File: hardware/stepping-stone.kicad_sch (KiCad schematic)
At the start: 0 parts

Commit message: Add MCU and USB symbols
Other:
- added sheet Microcontroller (microcontroller.kicad_sch)
- added sheet USB-C Interface (usb-interface.kicad_sch)
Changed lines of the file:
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@@
 	(generator_version "10.0")
 	(paper "A")
+	(sheet
+		(at 76.2 88.9)
+		(size 25.4 25.4)
+		(exclude_from_sim no)
+		(in_bom yes)
+		(on_board yes)
+		(dnp no)
+		(fields_autoplaced yes)
+		(stroke
+			(width 0.3048)
+			(type solid)
+		)
+		(fill
+			(color 255 229 191 1)
+		)
+		(property "Sheetname" "USB-C Interface"
+			(at 76.2 88.1122 0)
+			(show_name no)
+			(do_not_autoplace no)
+			(effects
+				(font
+					(size 1.27 1.27)
+				)
+				(justify left bottom)
+			)
+		)
+		(property "Sheetfile" "usb-interface.kicad_sch"
+			(at 76.2 114.9608 0)
+			(show_name no)
+			(do_not_autoplace no)
+			(effects
+				(font
+					(size 1.27 1.27)
+				)
+				(justify left top)
+			)
+		)
+		(instances
+			(project "stepping-stone"
+				(path "/793a882e-3f7b-468b-a863-41a1f527e1bf"
+					(page "3")
+				)
+			)
+		)
+	)
+	(sheet
+		(at 127 88.9)
+		(size 25.4 25.4)
+		(exclude_from_sim no)
+		(in_bom yes)
+		(on_board yes)
+		(dnp no)
+		(fields_autoplaced yes)
+		(stroke
+			(width 0.3048)
+			(type solid)
+		)
+		(fill
+			(color 255 229 191 1)
+		)
+		(property "Sheetname" "Microcontroller"
+			(at 127 88.1122 0)
+			(show_name no)
+			(do_not_autoplace no)
+			(effects
+				(font
+					(size 1.27 1.27)
+				)
+				(justify left bottom)
+			)
+		)
+		(property "Sheetfile" "microcontroller.kicad_sch"
+			(at 127 114.9608 0)
+			(show_name no)
+			(do_not_autoplace no)
+			(effects
+				(font
+					(size 1.27 1.27)
+				)
+				(justify left top)
+			)
+		)
+		(instances
+			(project "stepping-stone"
+				(path "/793a882e-3f7b-468b-a863-41a1f527e1bf"
+					(page "2")
+				)
+			)
+		)
+	)
 	(sheet_instances
 		(path "/"

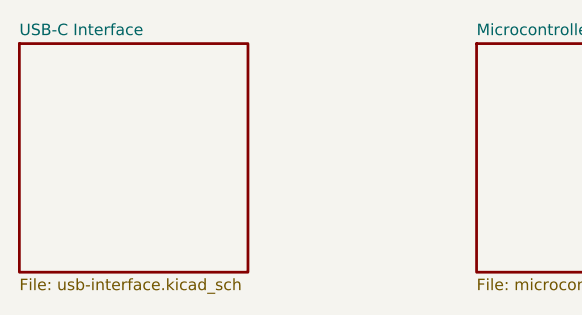
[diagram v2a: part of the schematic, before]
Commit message: Draft power inputs sheet
Added USB C PD input and external supply, with ideal diode ORing.
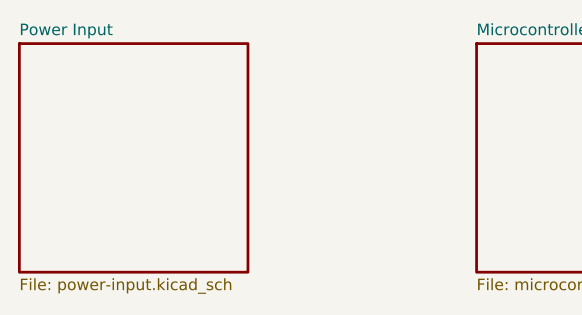
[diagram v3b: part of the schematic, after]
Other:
- sheet USB-C Interface renamed Power Input
- sheet Power Input: file usb-interface.kicad_sch -> power-input.kicad_sch
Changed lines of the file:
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@@
 			(color 255 229 191 1)
 		)
-		(property "Sheetname" "USB-C Interface"
+		(property "Sheetname" "Power Input"
 			(at 76.2 88.1122 0)
 			(show_name no)
@@
 			)
 		)
-		(property "Sheetfile" "usb-interface.kicad_sch"
+		(property "Sheetfile" "power-input.kicad_sch"
 			(at 76.2 114.9608 0)
 			(show_name no)

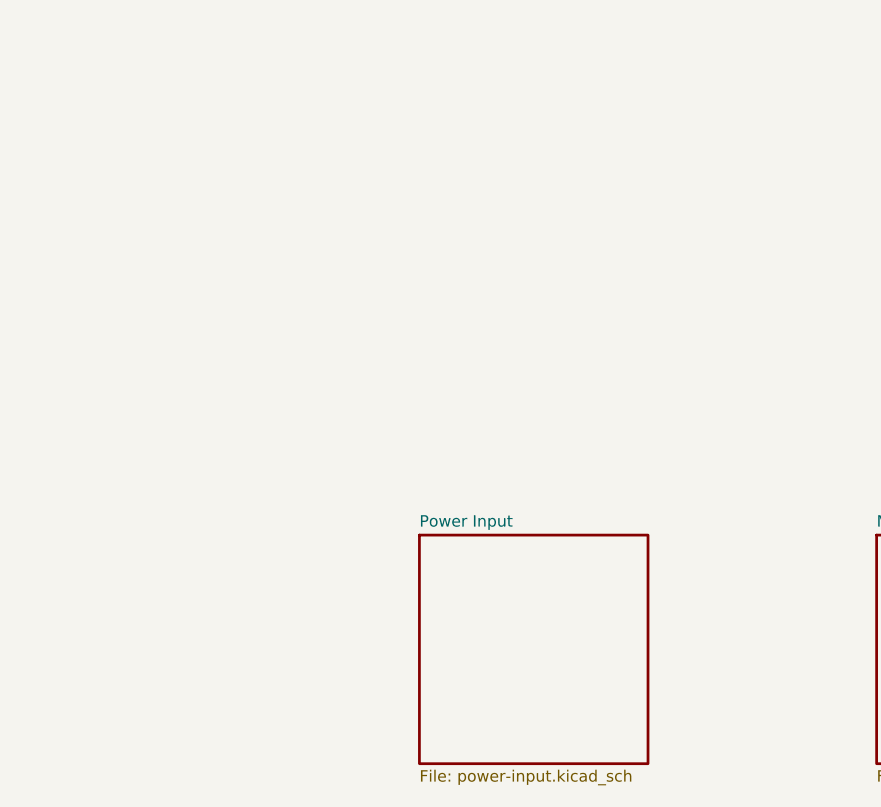
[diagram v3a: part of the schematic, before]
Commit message: Finalize source select
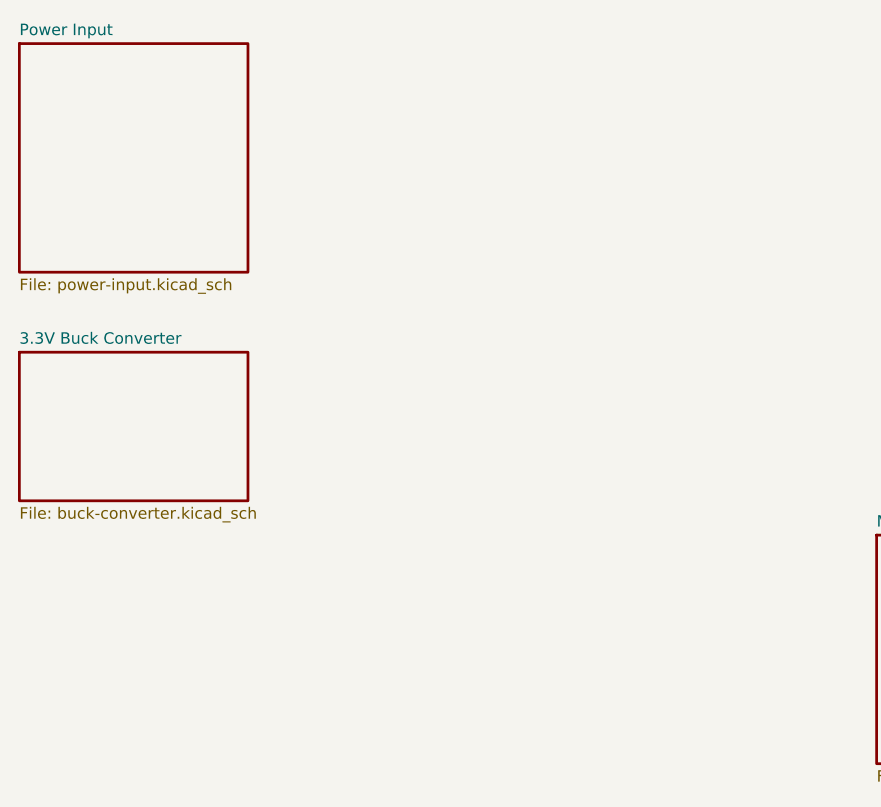
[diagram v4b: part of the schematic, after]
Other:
- added sheet 3.3V Buck Converter (buck-converter.kicad_sch)
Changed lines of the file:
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@@
 	(paper "A")
 	(sheet
-		(at 76.2 88.9)
+		(at 31.75 34.29)
 		(size 25.4 25.4)
 		(exclude_from_sim no)
@@
 		)
 		(property "Sheetname" "Power Input"
-			(at 76.2 88.1122 0)
+			(at 31.75 33.5022 0)
 			(show_name no)
 			(do_not_autoplace no)
@@
 		)
 		(property "Sheetfile" "power-input.kicad_sch"
-			(at 76.2 114.9608 0)
+			(at 31.75 60.3508 0)
 			(show_name no)
 			(do_not_autoplace no)
@@
 				)
 			)
+		)
+	)
+	(sheet
+		(at 31.75 68.58)
+		(size 25.4 16.51)
+		(exclude_from_sim no)
+		(in_bom yes)
+		(on_board yes)
+		(dnp no)
+		(fields_autoplaced yes)
+		(stroke
+			(width 0.3048)
+			(type solid)
+		)
+		(fill
+			(color 255 229 191 1)
+		)
+		(property "Sheetname" "3.3V Buck Converter"
+			(at 31.75 67.7922 0)
+			(show_name no)
+			(do_not_autoplace no)
+			(effects
+				(font
+					(size 1.27 1.27)
+				)
+				(justify left bottom)
+			)
+		)
+		(property "Sheetfile" "buck-converter.kicad_sch"
+			(at 31.75 85.7508 0)
+			(show_name no)
+			(do_not_autoplace no)
+			(effects
+				(font
+					(size 1.27 1.27)
+				)
+				(justify left top)
+			)
+		)
+		(instances
+			(project "stepping-stone"
+				(path "/793a882e-3f7b-468b-a863-41a1f527e1bf"
+					(page "4")
+				)
+			)

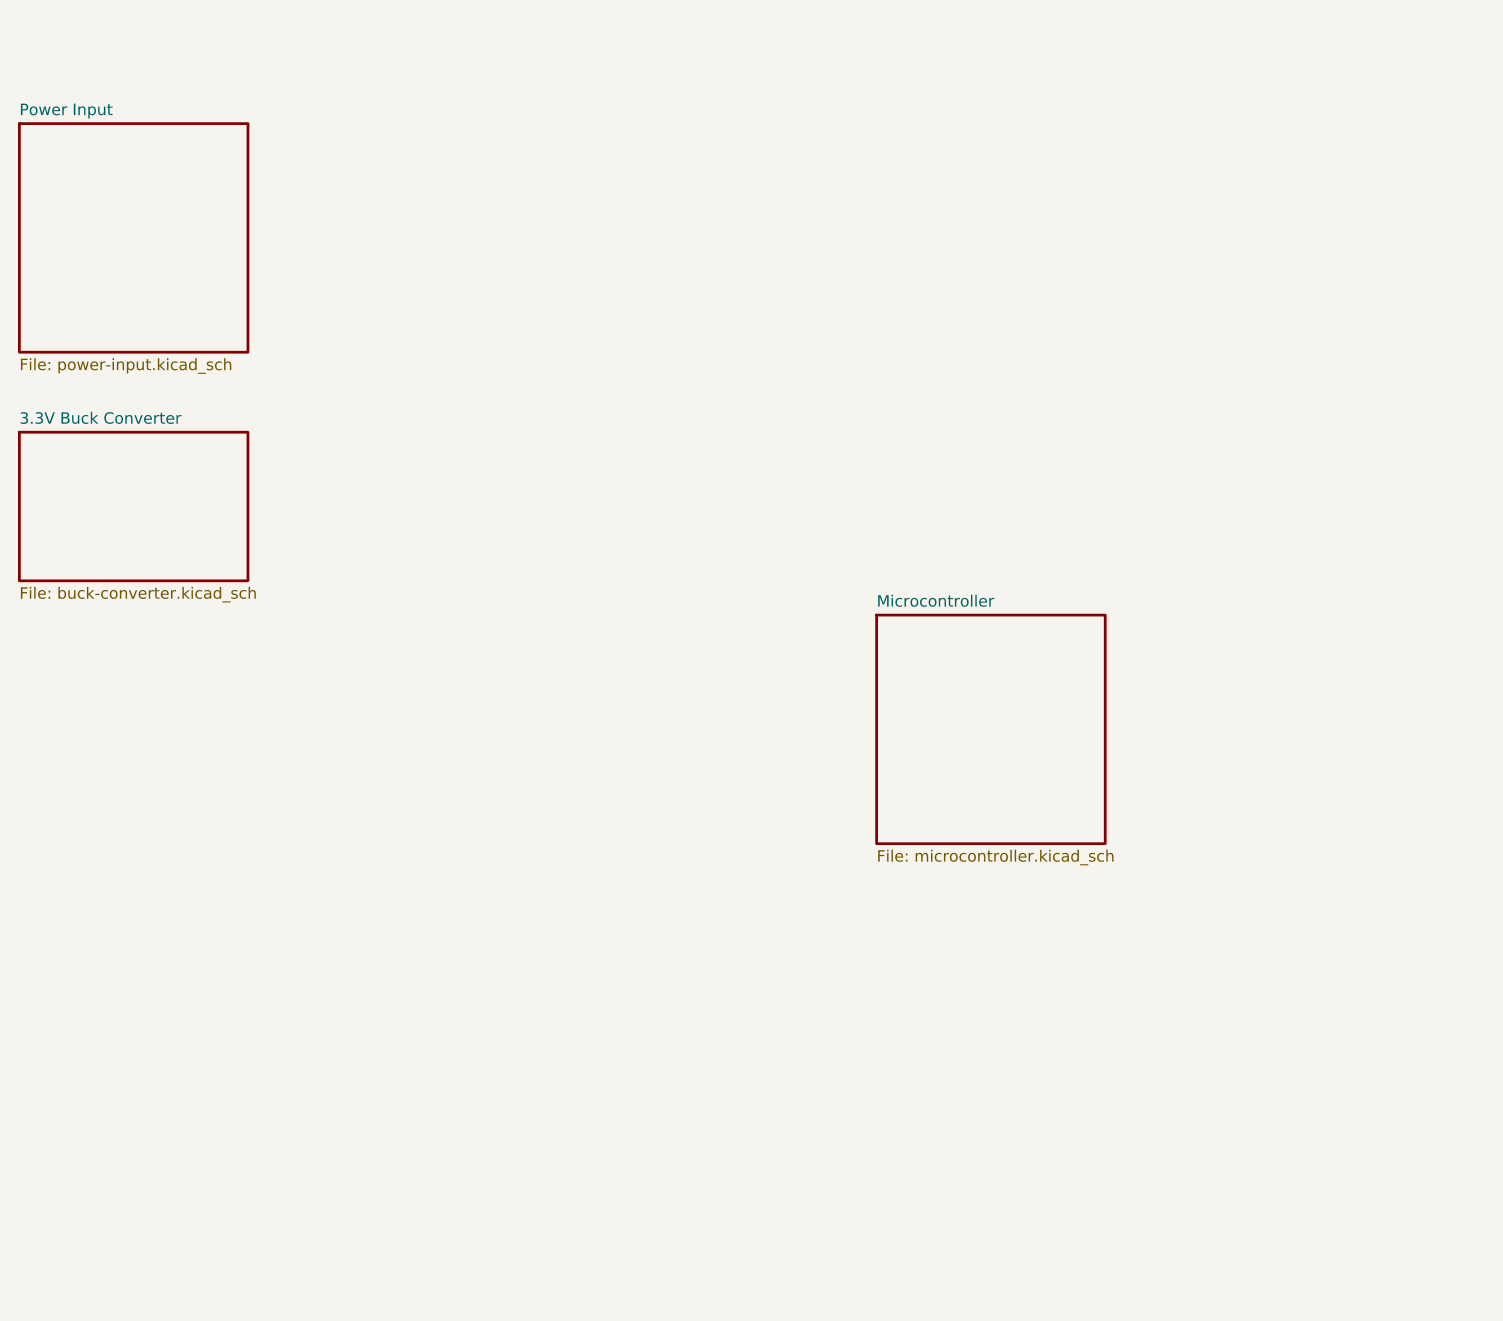
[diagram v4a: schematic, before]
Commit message: Add 3.3V buck converter
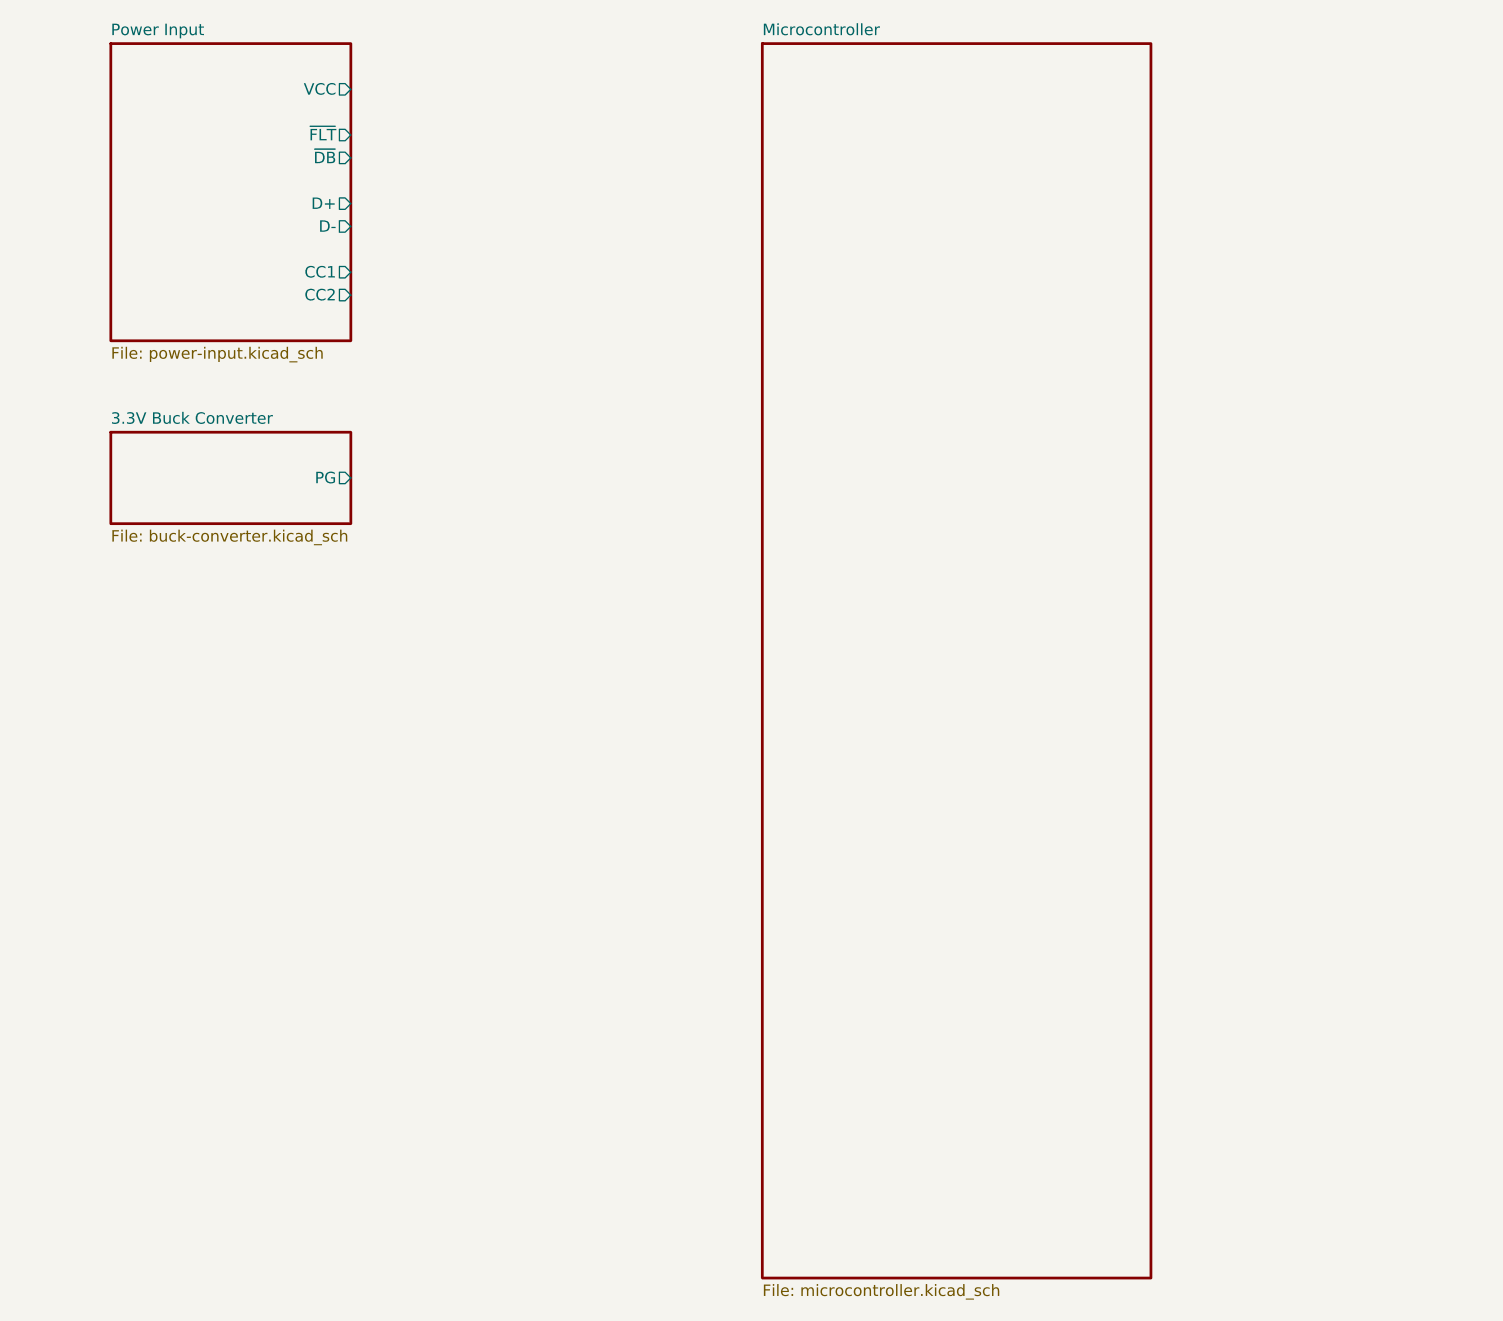
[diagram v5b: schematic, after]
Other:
- sheet 3.3V Buck Converter ports: added PG; removed none
- sheet Power Input ports: added CC1, CC2, D+, D-, VCC, ~{DB}, ~{FLT}; removed none
- company: (none) -> Jacob Wigent
- title: (none) -> Stepping-Stone - Stepper Motor Platform
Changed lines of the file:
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@@
 	(generator_version "10.0")
 	(paper "A")
+	(title_block
+		(title "Stepping-Stone - Stepper Motor Platform")
+		(rev "A")
+		(company "Jacob Wigent")
+	)
 	(sheet
-		(at 31.75 34.29)
-		(size 25.4 25.4)
+		(at 41.91 25.4)
+		(size 26.67 33.02)
 		(exclude_from_sim no)
 		(in_bom yes)
@@
 		)
 		(property "Sheetname" "Power Input"
-			(at 31.75 33.5022 0)
+			(at 41.91 24.6122 0)
 			(show_name no)
 			(do_not_autoplace no)
@@
 		)
 		(property "Sheetfile" "power-input.kicad_sch"
-			(at 31.75 60.3508 0)
+			(at 41.91 59.0808 0)
 			(show_name no)
 			(do_not_autoplace no)
@@
 				)
 				(justify left top)
+			)
+		)
+		(pin "CC1" output
+			(at 68.58 50.8 0)
+			(effects
+				(font
+					(size 1.27 1.27)
+				)
+				(justify right)
+			)
+		)
+		(pin "CC2" output
+			(at 68.58 53.34 0)
+			(effects
+				(font
+					(size 1.27 1.27)
+				)
+				(justify right)
+			)
+		)
+		(pin "D+" output
+			(at 68.58 43.18 0)
+			(effects
+				(font
+					(size 1.27 1.27)
+				)
+				(justify right)
+			)
+		)
+		(pin "D-" output
+			(at 68.58 45.72 0)
+			(effects
+				(font
+					(size 1.27 1.27)
+				)
+				(justify right)
+			)
+		)
+		(pin "VCC" output
+			(at 68.58 30.48 0)
+			(effects
+				(font
+					(size 1.27 1.27)
+				)
+				(justify right)
+			)
+		)
+		(pin "~{DB}" output
+			(at 68.58 38.1 0)
+			(effects
+				(font
+					(size 1.27 1.27)
+				)
+				(justify right)
+			)
+		)
+		(pin "~{FLT}" output
+			(at 68.58 35.56 0)
+			(effects
+				(font
+					(size 1.27 1.27)
+				)
+				(justify right)
 			)
 		)
@@
 	)
 	(sheet
-		(at 127 88.9)
-		(size 25.4 25.4)
+		(at 114.3 25.4)
+		(size 43.18 137.16)
 		(exclude_from_sim no)
 		(in_bom yes)
@@
 		)
 		(property "Sheetname" "Microcontroller"
-			(at 127 88.1122 0)
+			(at 114.3 24.6122 0)
 			(show_name no)
 			(do_not_autoplace no)
@@
 		)
 		(property "Sheetfile" "microcontroller.kicad_sch"
-			(at 127 114.9608 0)
+			(at 114.3 163.2208 0)
 			(show_name no)
 			(do_not_autoplace no)
@@
 	)
 	(sheet
-		(at 31.75 68.58)
-		(size 25.4 16.51)
+		(at 41.91 68.58)
+		(size 26.67 10.16)
 		(exclude_from_sim no)
 		(in_bom yes)
@@
 		)
 		(property "Sheetname" "3.3V Buck Converter"
-			(at 31.75 67.7922 0)
+			(at 41.91 67.7922 0)
 			(show_name no)
 			(do_not_autoplace no)
@@
 		)
 		(property "Sheetfile" "buck-converter.kicad_sch"
-			(at 31.75 85.7508 0)
+			(at 41.91 79.4008 0)
 			(show_name no)
 			(do_not_autoplace no)
@@
 			)
 		)
+		(pin "PG" output
+			(at 68.58 73.66 0)
+			(effects
+				(font
+					(size 1.27 1.27)
+				)
+				(justify right)
+			)
+		)

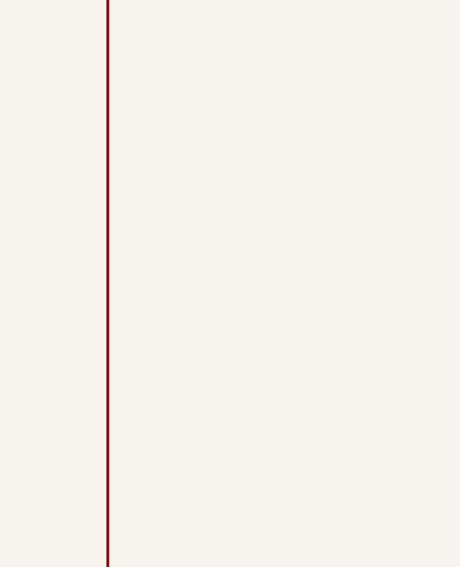
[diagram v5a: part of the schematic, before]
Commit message: Create MCU schematic
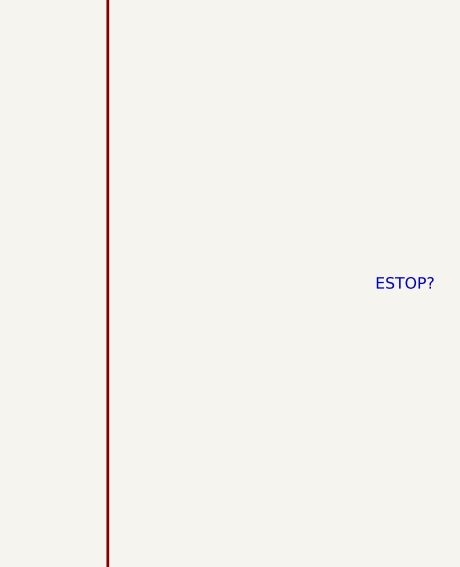
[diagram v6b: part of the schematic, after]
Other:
- note added: "ESTOP?"
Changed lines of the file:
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@@
 		(company "Jacob Wigent")
+	)
+	(text "ESTOP?"
+		(exclude_from_sim no)
+		(at 190.5 78.74 0)
+		(effects
+			(font
+				(size 1.27 1.27)
+				(color 194 0 0 1)
+			)
+		)
 	)
 	(sheet
